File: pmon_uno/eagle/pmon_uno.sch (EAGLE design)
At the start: 42 parts, among them J1 USB, J2 USB, J3 TERMINAL-2, Q1 16Mhz, U1 LTC2943, U2 FT232RL, U3 LT1764AEQ, U4 ATMEGA328TQFP32

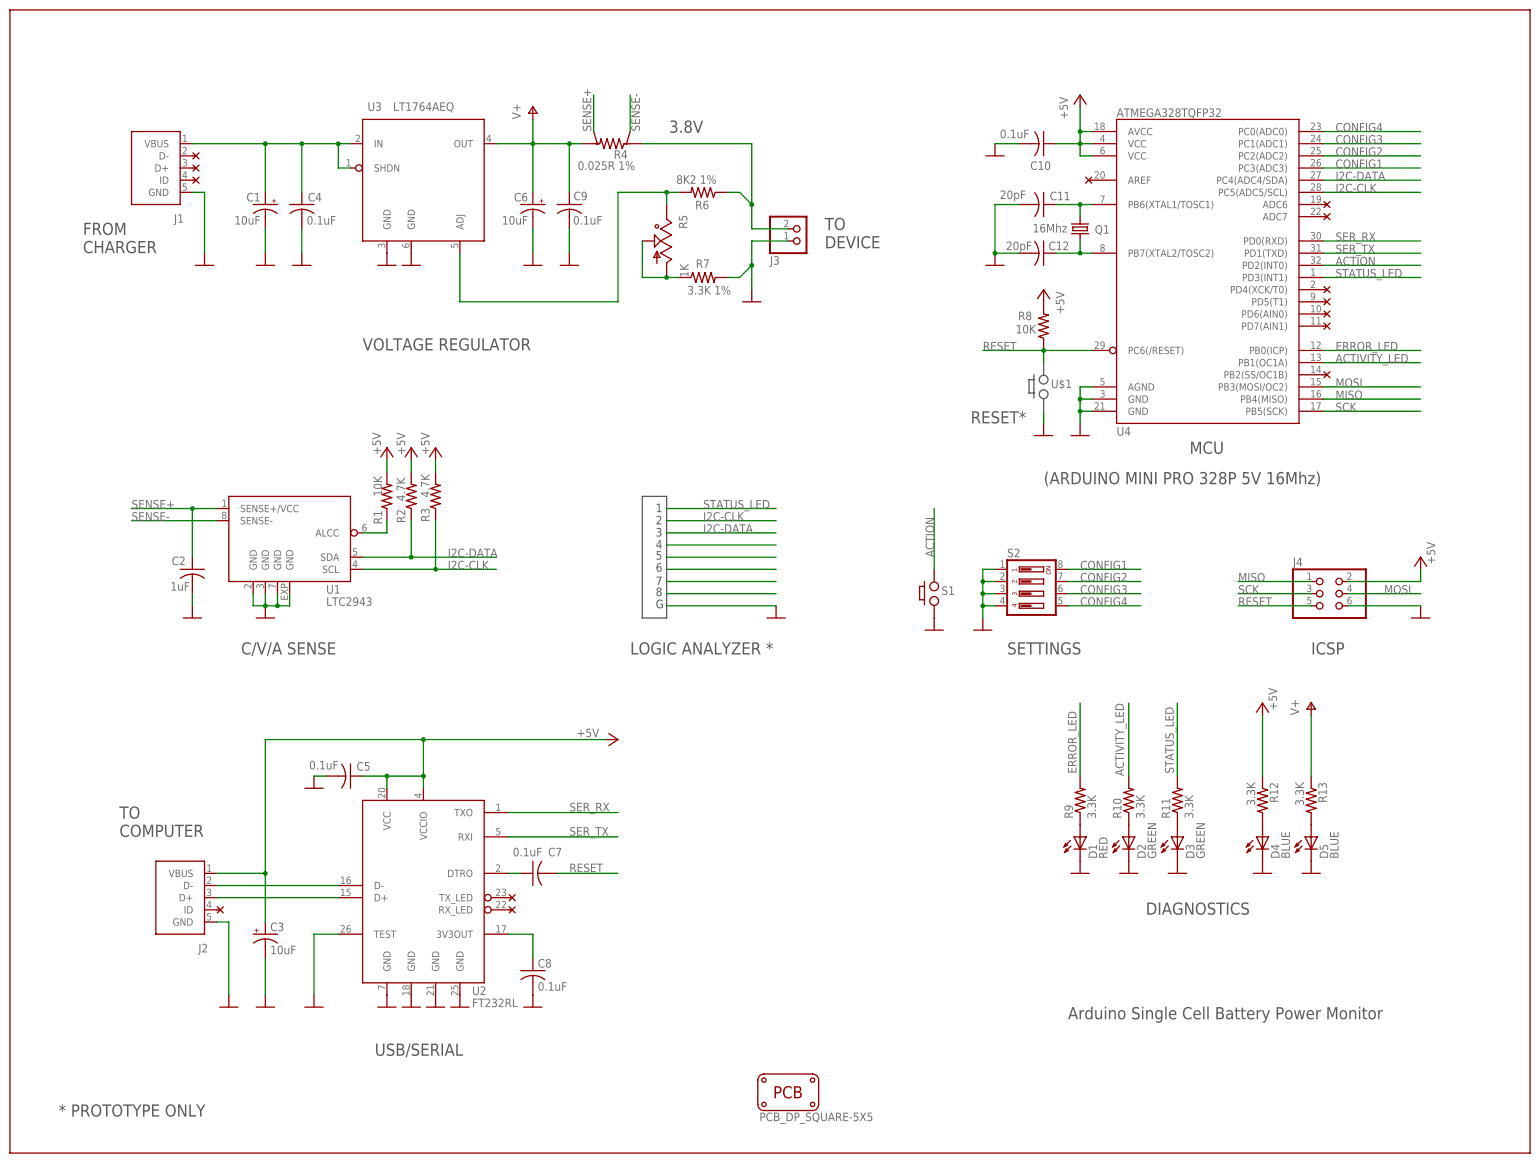
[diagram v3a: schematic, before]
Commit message: Changed the button and power terminals to be top access (incremented to Rev B), Yet to be auto routed.
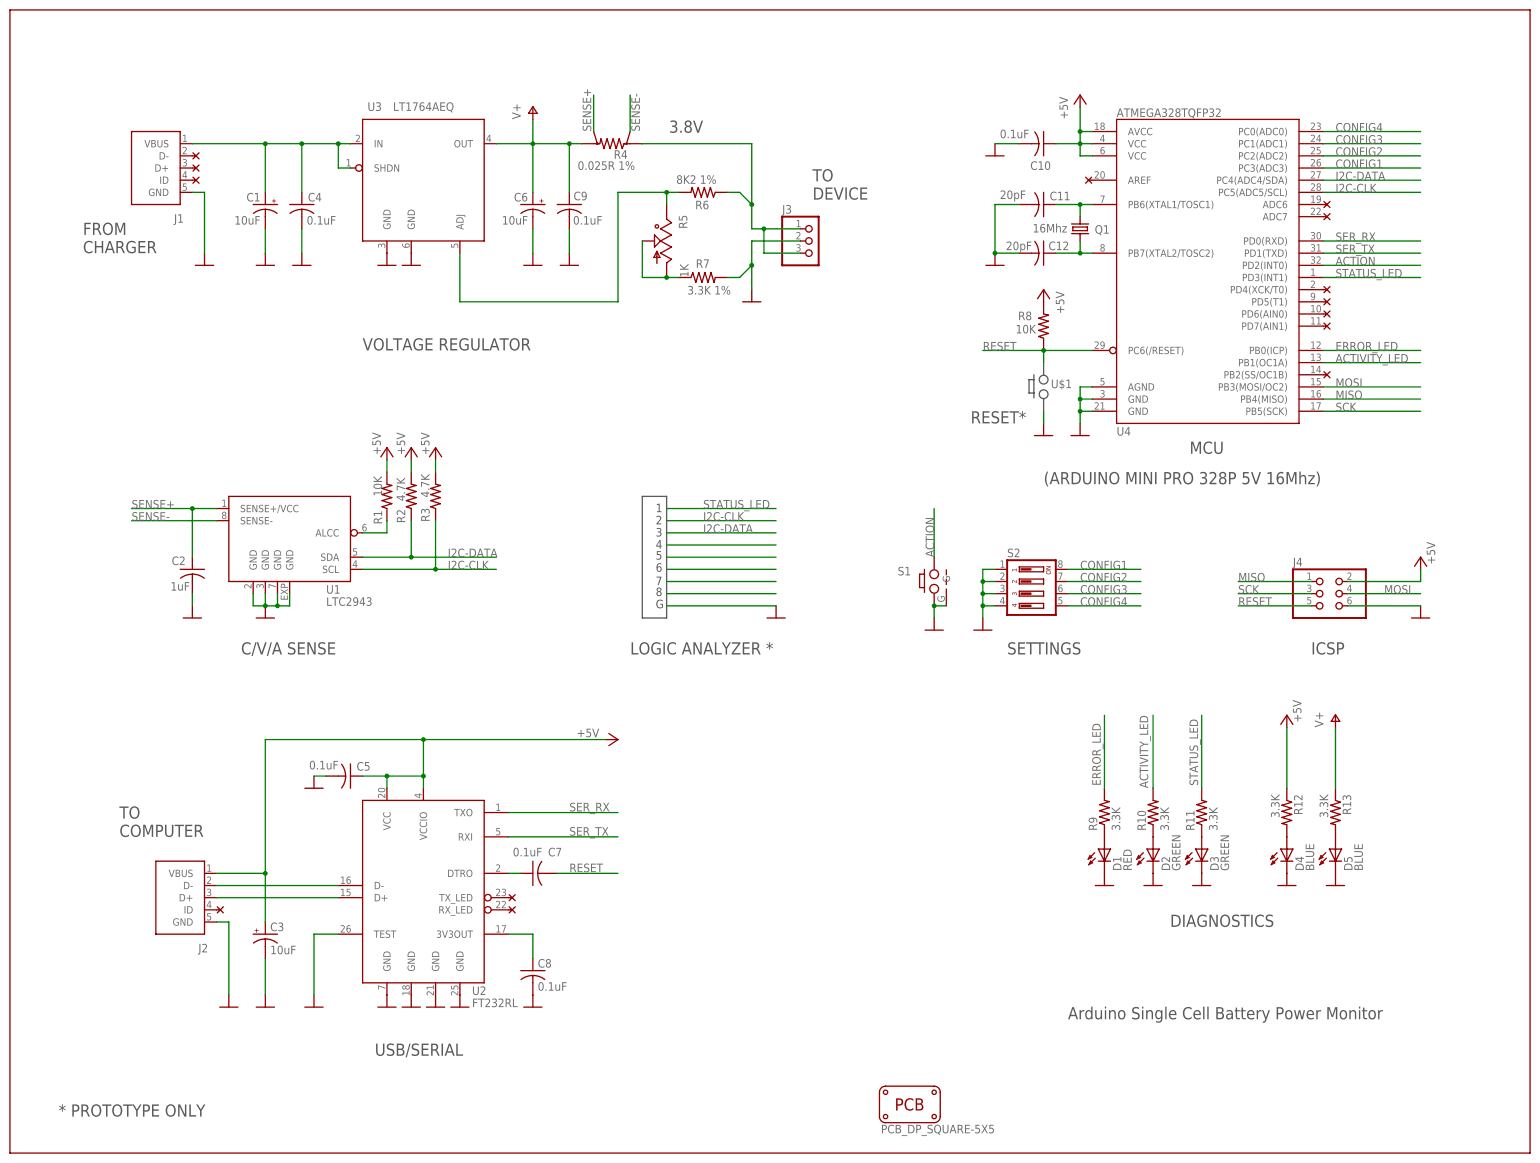
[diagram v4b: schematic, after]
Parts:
- J3: value TERMINAL-2 -> (none); device pmon_uno:TERMINAL-2 -> pmon_uno:PINHD-1X3
- S1: value PUSH_BUTTONEVQPSL -> PUSH_BUTTON_SHIELDED; device pmon_uno:PUSH_BUTTONEVQPSL -> pmon_uno:PUSH_BUTTON_SHIELDED
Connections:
- net GND: now also J3.2, S1.G; no longer J3.1
- net N$22: now also J3.1, J3.3; no longer J3.2
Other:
- moved on the sheet: D1, D2, D3, D4, D5, R10, R11, R12, R13, R9

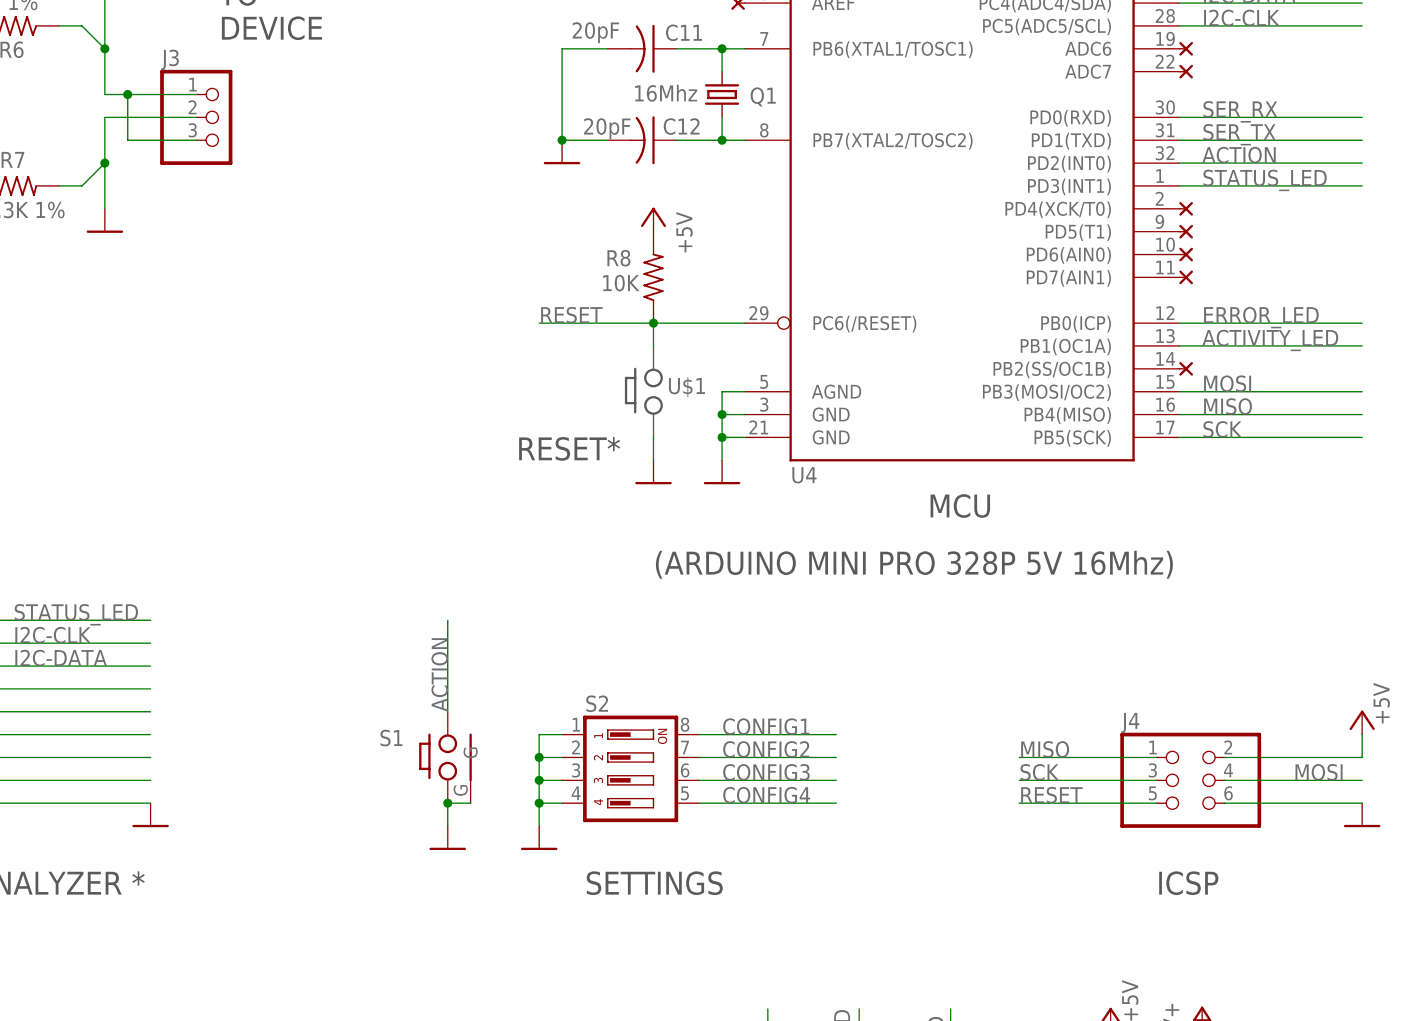
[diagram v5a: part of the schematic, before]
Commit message: Started to cleanup the pmon uno BOM.
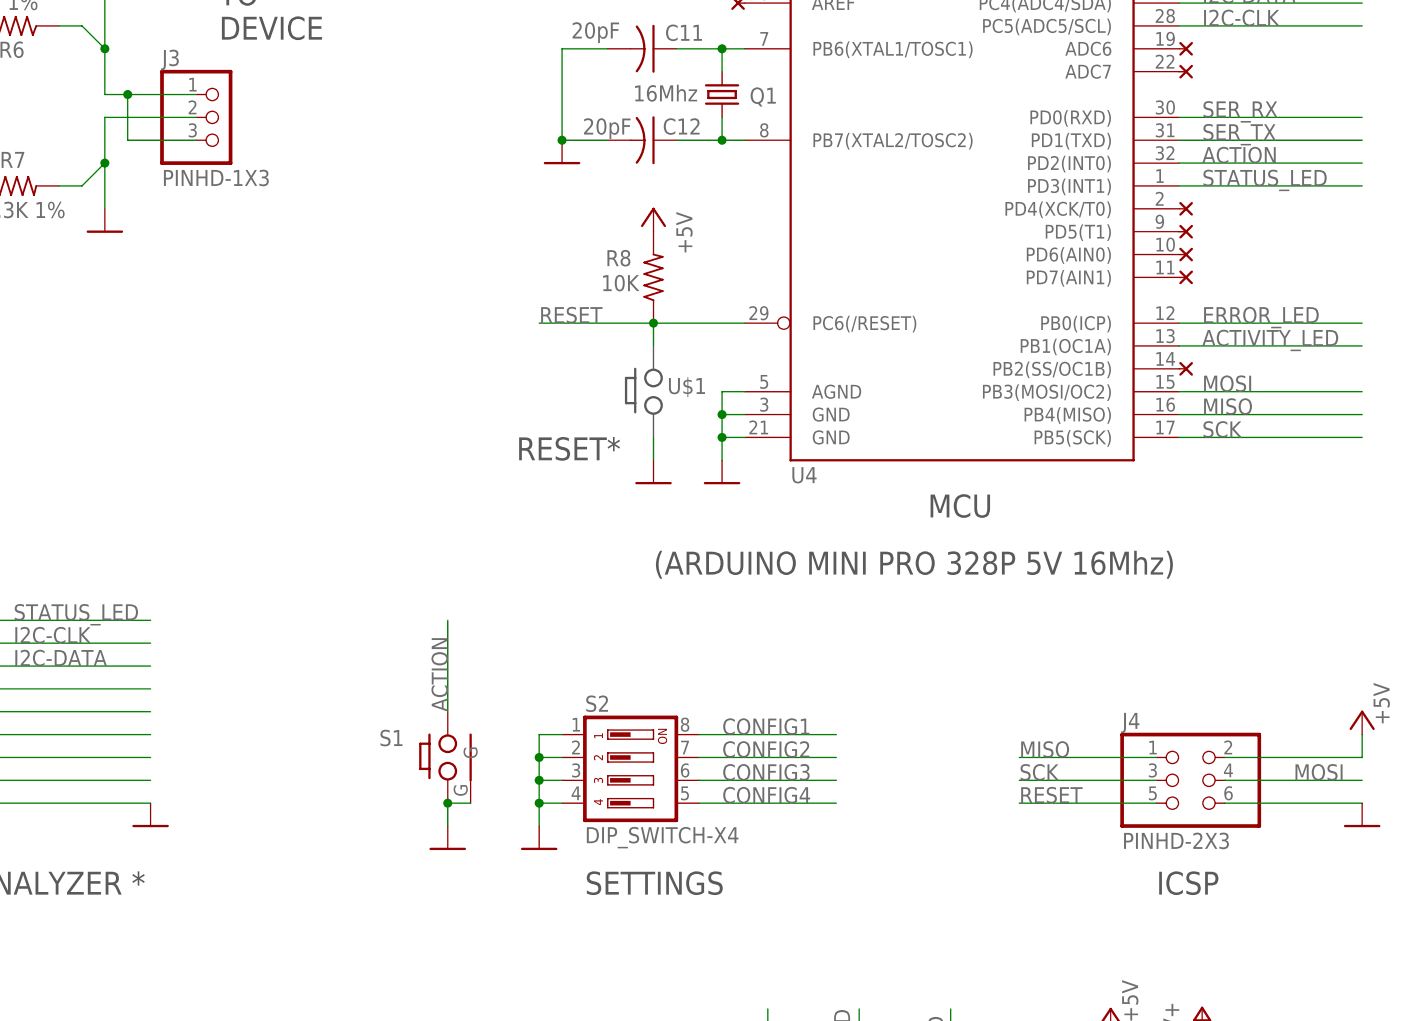
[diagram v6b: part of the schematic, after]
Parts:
- C10, C11, C12, C2, C4, C5, C7, C8, C9: device pmon_uno:C-USC0603 -> pmon_uno:CAP-C0603
- D1, D2, D3, D4, D5: device pmon_uno:LED -> pmon_uno:LED1206
- J3: value (none) -> PINHD-1X3
- J4: value (none) -> PINHD-2X3
- R1, R10, R11, R12, R13, R2, R3, R6, R7, R8, R9: device pmon_uno:R-US_R0603 -> pmon_uno:RES-R0603
- R4: device pmon_uno:SHUNT -> pmon_uno:RES-SHUNT-6432
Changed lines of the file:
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@@
 </classes>
 <parts>
-<part name="R9" library="pmon_uno" deviceset="R-US_" device="R0603" value="3.3K"/>
-<part name="R10" library="pmon_uno" deviceset="R-US_" device="R0603" value="3.3K"/>
+<part name="R9" library="pmon_uno" deviceset="RES-" device="R0603" value="3.3K"/>
+<part name="R10" library="pmon_uno" deviceset="RES-" device="R0603" value="3.3K"/>
 <part name="GND3" library="pmon_uno" deviceset="GND" device=""/>
-<part name="C7" library="pmon_uno" deviceset="C-US" device="C0603" value="0.1uF"/>
+<part name="C7" library="pmon_uno" deviceset="CAP-" device="C0603" value="0.1uF"/>
 <part name="P+2" library="pmon_uno" deviceset="+5V" device=""/>
 <part name="GND2" library="pmon_uno" deviceset="GND" device=""/>
 <part name="GND16" library="pmon_uno" deviceset="GND" device=""/>
-<part name="J4" library="pmon_uno" deviceset="PINHD-2X3" device=""/>
+<part name="J4" library="pmon_uno" deviceset="PINHD-2X3" device="" value="PINHD-2X3"/>
 <part name="GND14" library="pmon_uno" deviceset="GND" device=""/>
 <part name="P+5" library="pmon_uno" deviceset="+5V" device=""/>
 <part name="GND8" library="pmon_uno" deviceset="GND" device=""/>
-<part name="D1" library="pmon_uno" deviceset="LED" device="" value="RED"/>
-<part name="D2" library="pmon_uno" deviceset="LED" device="" value="GREEN"/>
-<part name="R8" library="pmon_uno" deviceset="R-US_" device="R0603" value="10K"/>
+<part name="D1" library="pmon_uno" deviceset="LED" device="1206" value="RED"/>
+<part name="D2" library="pmon_uno" deviceset="LED" device="1206" value="GREEN"/>
+<part name="R8" library="pmon_uno" deviceset="RES-" device="R0603" value="10K"/>
 <part name="P+1" library="pmon_uno" deviceset="+5V" device=""/>
-<part name="C10" library="pmon_uno" deviceset="C-US" device="C0603" value="0.1uF"/>
+<part name="C10" library="pmon_uno" deviceset="CAP-" device="C0603" value="0.1uF"/>
 <part name="C3" library="pmon_uno" deviceset="CPOL-US" device="A/3216-18R" value="10uF"/>
 <part name="GND1" library="pmon_uno" deviceset="GND" device=""/>
-<part name="D4" library="pmon_uno" deviceset="LED" device="" value="BLUE"/>
-<part name="R12" library="pmon_uno" deviceset="R-US_" device="R0603" value="3.3K"/>
+<part name="D4" library="pmon_uno" deviceset="LED" device="1206" value="BLUE"/>
+<part name="R12" library="pmon_uno" deviceset="RES-" device="R0603" value="3.3K"/>
 <part name="P+4" library="pmon_uno" deviceset="+5V" device=""/>
-<part name="C8" library="pmon_uno" deviceset="C-US" device="C0603" value="0.1uF"/>
-<part name="C5" library="pmon_uno" deviceset="C-US" device="C0603" value="0.1uF"/>
+<part name="C8" library="pmon_uno" deviceset="CAP-" device="C0603" value="0.1uF"/>
+<part name="C5" library="pmon_uno" deviceset="CAP-" device="C0603" value="0.1uF"/>
 <part name="U$3" library="pmon_uno" deviceset="NC" device=""/>
 <part name="GND5" library="pmon_uno" deviceset="GND" device=""/>
@@
 <part name="GND20" library="pmon_uno" deviceset="GND" device=""/>
 <part name="GND21" library="pmon_uno" deviceset="GND" device=""/>
-<part name="R6" library="pmon_uno" deviceset="R-US_" device="R0603" value="8K2 1%"/>
-<part name="R7" library="pmon_uno" deviceset="R-US_" device="R0603" value="3.3K 1%"/>
+<part name="R6" library="pmon_uno" deviceset="RES-" device="R0603" value="8K2 1%"/>
+<part name="R7" library="pmon_uno" deviceset="RES-" device="R0603" value="3.3K 1%"/>
 <part name="GND23" library="pmon_uno" deviceset="GND" device=""/>
 <part name="C6" library="pmon_uno" deviceset="CPOL-US" device="A/3216-18R" value="10uF"/>
 <part name="C1" library="pmon_uno" deviceset="CPOL-US" device="A/3216-18R" value="10uF"/>
 <part name="GND24" library="pmon_uno" deviceset="GND" device=""/>
-<part name="C4" library="pmon_uno" deviceset="C-US" device="C0603" value="0.1uF"/>
+<part name="C4" library="pmon_uno" deviceset="CAP-" device="C0603" value="0.1uF"/>
 <part name="GND25" library="pmon_uno" deviceset="GND" device=""/>
-<part name="C9" library="pmon_uno" deviceset="C-US" device="C0603" value="0.1uF"/>
+<part name="C9" library="pmon_uno" deviceset="CAP-" device="C0603" value="0.1uF"/>
 <part name="GND26" library="pmon_uno" deviceset="GND" device=""/>
 <part name="GND27" library="pmon_uno" deviceset="GND" device=""/>
-<part name="C2" library="pmon_uno" deviceset="C-US" device="C0603" value="1uF"/>
+<part name="C2" library="pmon_uno" deviceset="CAP-" device="C0603" value="1uF"/>
 <part name="P+9" library="pmon_uno" deviceset="V+" device=""/>
-<part name="R4" library="pmon_uno" deviceset="SHUNT" device="" value="0.025R 1%"/>
-<part name="R2" library="pmon_uno" deviceset="R-US_" device="R0603" value="4.7K"/>
-<part name="R3" library="pmon_uno" deviceset="R-US_" device="R0603" value="4.7K"/>
+<part name="R4" library="pmon_uno" deviceset="RES-SHUNT-" device="6432" value="0.025R 1%"/>
+<part name="R2" library="pmon_uno" deviceset="RES-" device="R0603" value="4.7K"/>
+<part name="R3" library="pmon_uno" deviceset="RES-" device="R0603" value="4.7K"/>
 <part name="P+11" library="pmon_uno" deviceset="+5V" device=""/>
 <part name="P+12" library="pmon_uno" deviceset="+5V" device=""/>
@@
 <part name="U1" library="pmon_uno" deviceset="LTC2943" device="" value="LTC2943"/>
 <part name="GND17" library="pmon_uno" deviceset="GND" device=""/>
-<part name="D5" library="pmon_uno" deviceset="LED" device="" value="BLUE"/>
-<part name="R13" library="pmon_uno" deviceset="R-US_" device="R0603" value="3.3K"/>
+<part name="D5" library="pmon_uno" deviceset="LED" device="1206" value="BLUE"/>
+<part name="R13" library="pmon_uno" deviceset="RES-" device="R0603" value="3.3K"/>
 <part name="GND28" library="pmon_uno" deviceset="GND" device=""/>
 <part name="P+8" library="pmon_uno" deviceset="V+" device=""/>
 <part name="GND31" library="pmon_uno" deviceset="GND" device=""/>
-<part name="R1" library="pmon_uno" deviceset="R-US_" device="R0603" value="10K"/>
+<part name="R1" library="pmon_uno" deviceset="RES-" device="R0603" value="10K"/>
 <part name="P+10" library="pmon_uno" deviceset="+5V" device=""/>
-<part name="D3" library="pmon_uno" deviceset="LED" device="" value="GREEN"/>
+<part name="D3" library="pmon_uno" deviceset="LED" device="1206" value="GREEN"/>
 <part name="GND32" library="pmon_uno" deviceset="GND" device=""/>
-<part name="R11" library="pmon_uno" deviceset="R-US_" device="R0603" value="3.3K"/>
+<part name="R11" library="pmon_uno" deviceset="RES-" device="R0603" value="3.3K"/>
 <part name="GND22" library="pmon_uno" deviceset="GND" device=""/>
 <part name="J2" library="pmon_uno" deviceset="USB" device=""/>
 <part name="Q1" library="pmon_uno" deviceset="CRYSTAL" device="CTS406" value="16Mhz"/>
-<part name="C11" library="pmon_uno" deviceset="C-US" device="C0603" value="20pF"/>
-<part name="C12" library="pmon_uno" deviceset="C-US" device="C0603" value="20pF"/>
+<part name="C11" library="pmon_uno" deviceset="CAP-" device="C0603" value="20pF"/>
+<part name="C12" library="pmon_uno" deviceset="CAP-" device="C0603" value="20pF"/>
 <part name="U$1" library="pmon_uno" deviceset="PUSH_BUTTON_GHOST" device=""/>
 <part name="PCB1" library="pmon_uno" deviceset="PCB_DP_SQUARE" device="-5X5"/>
@@
 <part name="U$9" library="pmon_uno" deviceset="NC" device=""/>
 <part name="S1" library="pmon_uno" deviceset="PUSH_BUTTON_SHIELDED" device=""/>
-<part name="J3" library="pmon_uno" deviceset="PINHD-1X3" device=""/>
+<part name="J3" library="pmon_uno" deviceset="PINHD-1X3" device="" value="PINHD-1X3"/>
 </parts>
 <sheets>
@@
 <instance part="GND2" gate="1" x="203.2" y="55.88"/>
 <instance part="GND16" gate="1" x="187.96" y="149.86"/>
-<instance part="J4" gate="A" x="238.76" y="116.84"/>
+<instance part="J4" gate="A" x="238.76" y="116.84" smashed="yes">
+<attribute name="NAME" x="232.41" y="122.555" size="1.778" layer="95"/>
+<attribute name="VALUE" x="232.41" y="109.22" size="1.778" layer="96"/>
+</instance>
 <instance part="GND14" gate="1" x="259.08" y="111.76"/>
 <instance part="P+5" gate="1" x="259.08" y="124.46" smashed="yes">
@@
 </instance>
 <instance part="GND29" gate="1" x="124.46" y="111.76"/>
-<instance part="S2" gate="G$1" x="177.8" y="119.38" smashed="yes" rot="R270">
-<attribute name="NAME" x="172.72" y="124.46" size="1.778" layer="95"/>
-</instance>
+<instance part="S2" gate="G$1" x="177.8" y="119.38" rot="R270"/>
 <instance part="GND30" gate="1" x="167.64" y="109.22"/>
 <instance part="J1" gate="G$1" x="-5.08" y="200.66"/>
